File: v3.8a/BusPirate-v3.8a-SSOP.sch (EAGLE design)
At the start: 40 parts, among them IC1 PIC24FJ64GA002, IC3 4066, IC4 IC_FT230X-SSOP-16, J1 CON-USB-F-MINI-B

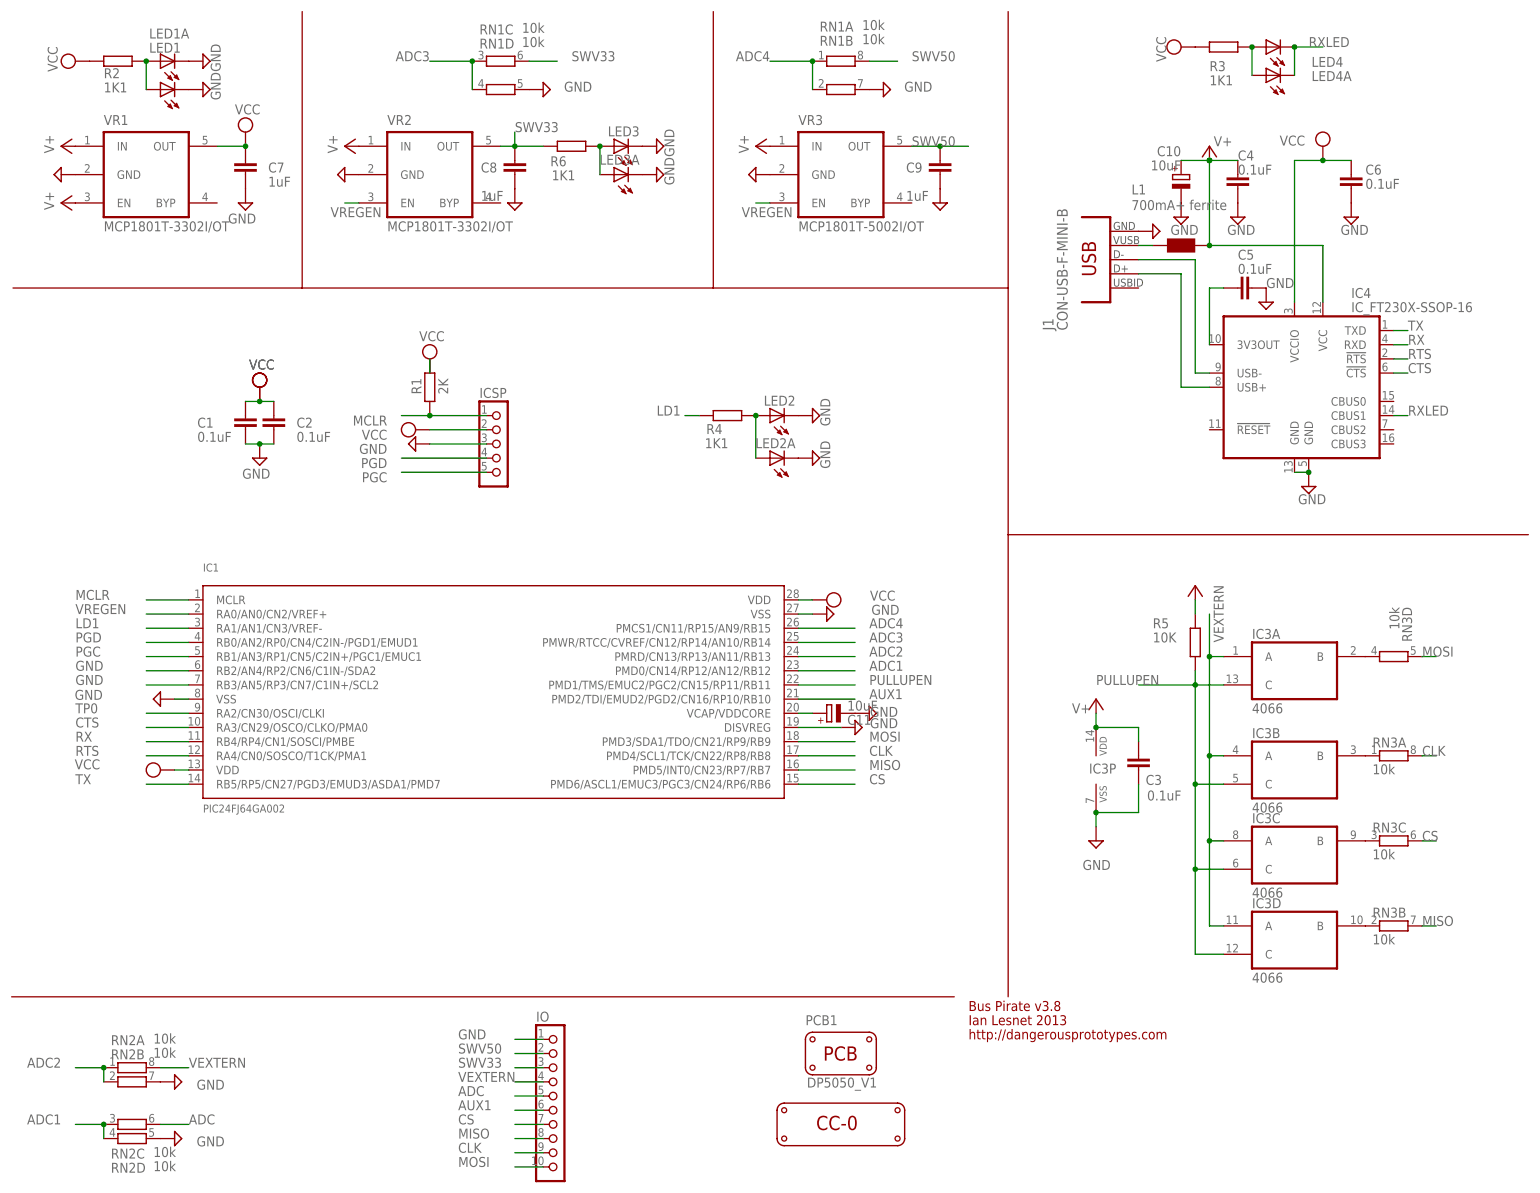
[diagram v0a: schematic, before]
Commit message: -replaced SMD version for the IO and ICSP header -fixed over hang distance of header including USB connector to 1.25mm -gerber generated
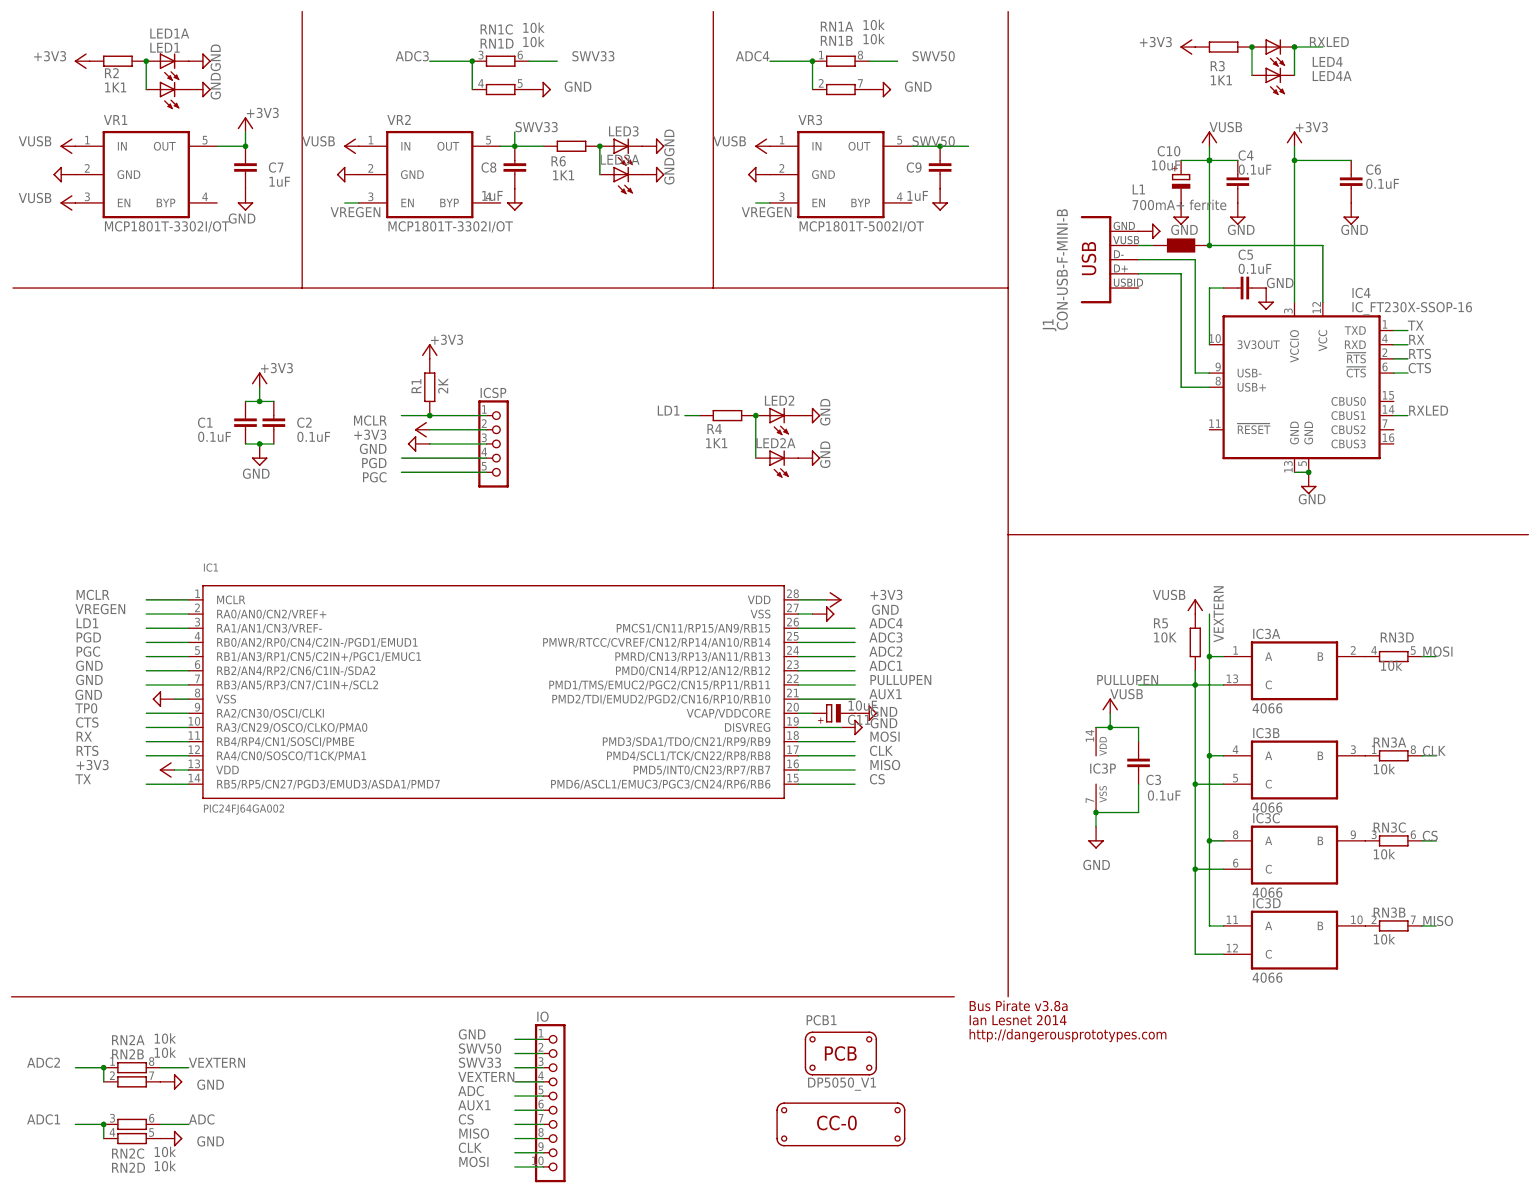
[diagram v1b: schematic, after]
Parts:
- ICSP: value CON_HEADER_1X05-PTH_RIGHT_ANGLED_B -> CON_HEADER_1X05-SMD_RIGHT_ANGLED_MALE_B; device dp_devices.v6:CON_HEADER_1X05-PTH_RIGHT_ANGLED_B -> dp_devices.v6:CON_HEADER_1X05-SMD_RIGHT_ANGLED_MALE_B
- IO: value CON_HEADER_1X10-RIGHT_ANGLED_PTH -> CON_HEADER_1X10-_RIGHTANGLED_SMD; device dp_devices.v6:CON_HEADER_1X10-RIGHT_ANGLED_PTH -> dp_devices.v6:CON_HEADER_1X10-_RIGHTANGLED_SMD
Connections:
- net V+ renamed VUSB
- net VCC renamed +3V3
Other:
- note added: "Bus Pirate v3.8a"
- note added: "Ian Lesnet 2014"
- note removed: "Bus Pirate v3.8"
- note removed: "Ian Lesnet 2013"

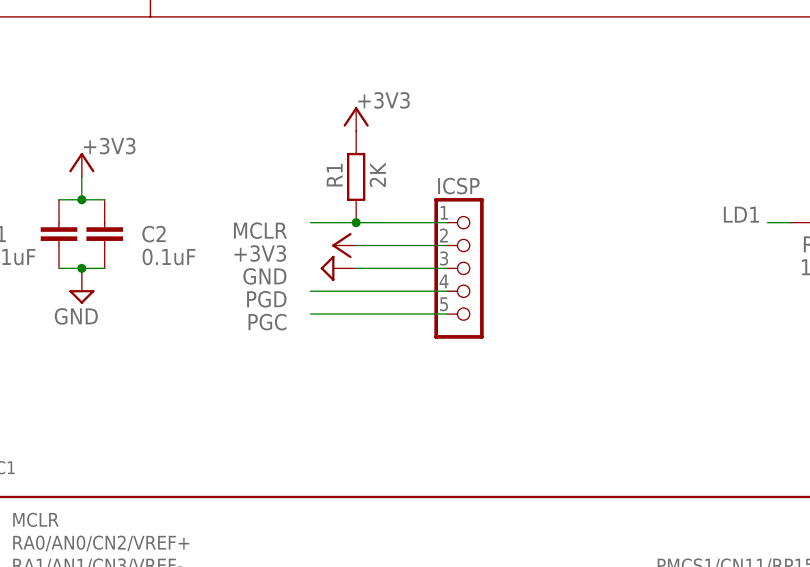
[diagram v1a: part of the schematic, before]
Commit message: board update: -changed ICSP header to 6pins, spare pin not connected -moved all LEDs a little to the right for even space
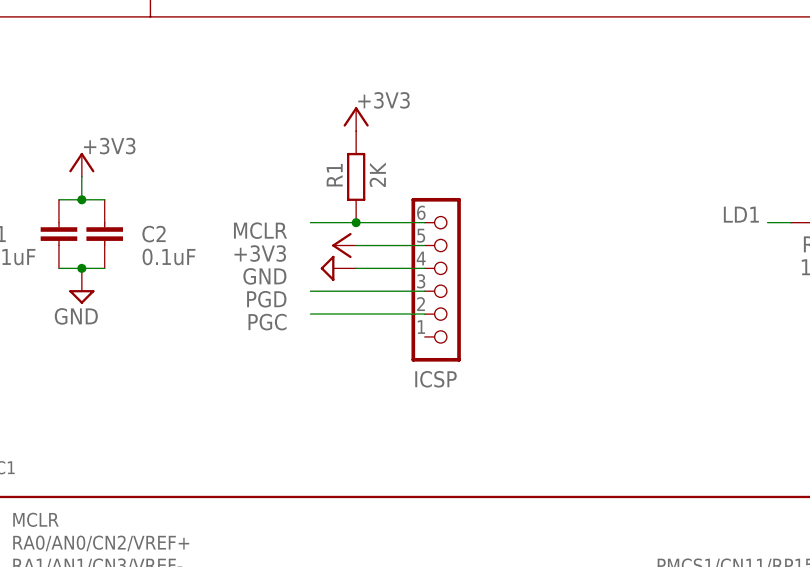
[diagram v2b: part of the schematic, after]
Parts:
- ICSP: value CON_HEADER_1X05-SMD_RIGHT_ANGLED_MALE_B -> CON_HEADER_1X06-SMD-RIGHT-ANGLED; device dp_devices.v6:CON_HEADER_1X05-SMD_RIGHT_ANGLED_MALE_B -> dp_devices.v6:CON_HEADER_1X06-SMD-RIGHT-ANGLED
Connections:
- net +3V3: now also ICSP.5; no longer ICSP.2
- net GND: now also ICSP.4; no longer ICSP.3
- net MCLR: now also ICSP.6; no longer ICSP.1
- net PGC: now also ICSP.2; no longer ICSP.5
- net PGD: now also ICSP.3; no longer ICSP.4
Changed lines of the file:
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@@
 <part name="VR2" library="dp_devices" deviceset="MIC5205" device="" value="MCP1801T-3302I/OT"/>
 <part name="VR3" library="dp_devices" deviceset="MIC5205" device="" value="MCP1801T-5002I/OT"/>
-<part name="ICSP" library="dp_devices.v6" deviceset="CON_HEADER_1X05" device="-SMD_RIGHT_ANGLED_MALE_B"/>
 <part name="LOGO1" library="dp_devices" deviceset="LOGO_CC-0" device=""/>
 <part name="J1" library="dp_devices.v6" deviceset="CON-USB-F" device="-MINI-B"/>
@@
 <part name="+3V8" library="dp_devices.v6" deviceset="SUPPLY_+3V3" device=""/>
 <part name="+3V9" library="dp_devices.v6" deviceset="SUPPLY_+3V3" device=""/>
+<part name="ICSP" library="dp_devices.v6" deviceset="CON_HEADER_1X06" device="-SMD-RIGHT-ANGLED"/>
 </parts>
 <sheets>
@@
 <instance part="VR2" gate="G$1" x="76.2" y="182.88"/>
 <instance part="VR3" gate="G$1" x="149.86" y="182.88"/>
-<instance part="ICSP" gate="J" x="86.36" y="134.62"/>
 <instance part="LOGO1" gate="LOGO" x="149.86" y="12.7"/>
 <instance part="J1" gate="USB" x="198.12" y="167.64" smashed="yes">
@@
 <instance part="+3V8" gate="G$1" x="15.24" y="203.2" smashed="yes" rot="R90"/>
 <instance part="+3V9" gate="G$1" x="213.36" y="205.74" smashed="yes" rot="R90"/>
+<instance part="ICSP" gate="J" x="83.82" y="132.08" rot="MR180"/>
 </instances>
 <busses>
@@
 <net name="GND" class="0">
 <segment>
-<wire x1="76.2" y1="134.62" x2="86.36" y2="134.62" width="0.1524" layer="91"/>
 <pinref part="V12" gate="GND" pin="GND"/>
-<pinref part="ICSP" gate="J" pin="3"/>
+<pinref part="ICSP" gate="J" pin="4"/>
+<wire x1="83.82" y1="134.62" x2="76.2" y2="134.62" width="0.1524" layer="91"/>
 </segment>
 <segment>
@@
 <segment>
 <wire x1="76.2" y1="139.7" x2="71.12" y2="139.7" width="0.1524" layer="91"/>
-<wire x1="86.36" y1="139.7" x2="76.2" y2="139.7" width="0.1524" layer="91"/>
 <junction x="76.2" y="139.7"/>
 <label x="68.58" y="139.7" size="1.778" layer="95" rot="R180"/>
 <pinref part="R1" gate="G$1" pin="1"/>
-<pinref part="ICSP" gate="J" pin="1"/>
+<pinref part="ICSP" gate="J" pin="6"/>
+<wire x1="76.2" y1="139.7" x2="83.82" y2="139.7" width="0.1524" layer="91"/>
 </segment>
 <segment>
@@
 </segment>
 <segment>
-<wire x1="71.12" y1="132.08" x2="86.36" y2="132.08" width="0.1524" layer="91"/>
 <label x="68.58" y="132.08" size="1.778" layer="95" rot="R180"/>
-<pinref part="ICSP" gate="J" pin="4"/>
+<pinref part="ICSP" gate="J" pin="3"/>
+<wire x1="83.82" y1="132.08" x2="71.12" y2="132.08" width="0.1524" layer="91"/>
 </segment>
 </net>
@@
 </segment>
 <segment>
-<wire x1="71.12" y1="129.54" x2="86.36" y2="129.54" width="0.1524" layer="91"/>
 <label x="68.58" y="129.54" size="1.778" layer="95" rot="R180"/>
-<pinref part="ICSP" gate="J" pin="5"/>
+<pinref part="ICSP" gate="J" pin="2"/>
+<wire x1="83.82" y1="129.54" x2="71.12" y2="129.54" width="0.1524" layer="91"/>
 </segment>
 </net>
@@
 </segment>
 <segment>
-<wire x1="86.36" y1="137.16" x2="76.2" y2="137.16" width="0.1524" layer="91"/>
-<pinref part="ICSP" gate="J" pin="2"/>
 <pinref part="+3V7" gate="G$1" pin="+3V3"/>
 <label x="68.58" y="137.16" size="1.778" layer="95" rot="R180"/>
-</segment>
-<segment>
+<pinref part="ICSP" gate="J" pin="5"/>
+<wire x1="83.82" y1="137.16" x2="76.2" y2="137.16" width="0.1524" layer="91"/>
+</segment>
+<segment>
